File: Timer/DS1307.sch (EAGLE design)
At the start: 6 parts, among them IC10 DS1307, Q4 32.768

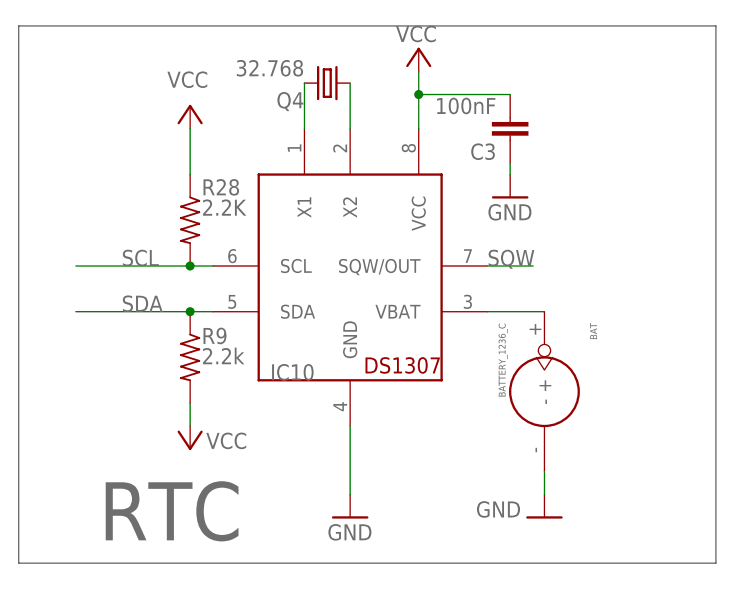
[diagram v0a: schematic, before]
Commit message: vcc updated in the circuit
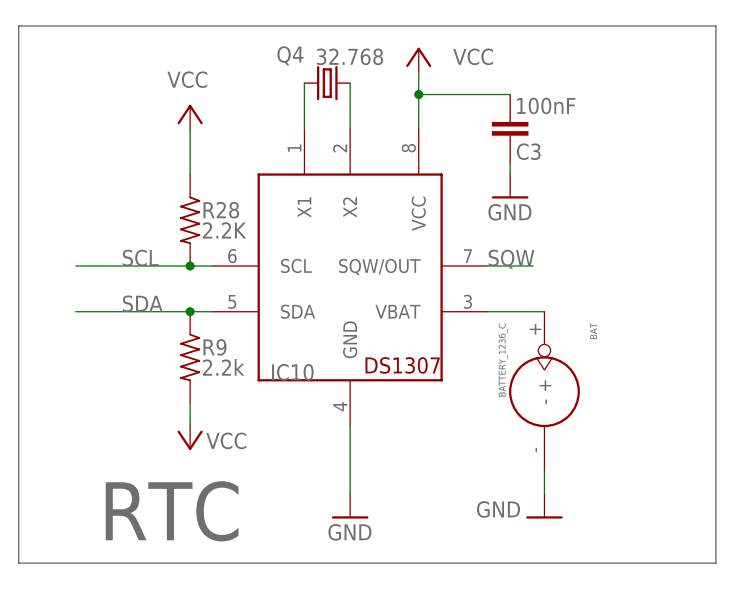
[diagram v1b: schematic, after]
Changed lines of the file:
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@@
 <layer number="94" name="Symbols" color="4" fill="1" visible="yes" active="yes"/>
 <layer number="95" name="Names" color="7" fill="1" visible="yes" active="yes"/>
-<layer number="96" name="Values" color="7" fill="1" visible="no" active="yes"/>
+<layer number="96" name="Values" color="7" fill="1" visible="yes" active="yes"/>
 <layer number="97" name="Info" color="7" fill="1" visible="yes" active="yes"/>
 <layer number="98" name="Guide" color="6" fill="1" visible="yes" active="yes"/>
@@
 <instances>
 <instance part="Q4" gate="G$1" x="-2.54" y="21.59" smashed="yes" rot="R180">
-<attribute name="NAME" x="-5.08" y="20.574" size="1.778" layer="95" rot="R180"/>
-<attribute name="VALUE" x="-5.08" y="24.13" size="1.778" layer="96" rot="R180"/>
+<attribute name="NAME" x="-5.08" y="25.654" size="1.778" layer="95" rot="R180"/>
+<attribute name="VALUE" x="3.81" y="25.4" size="1.778" layer="96" rot="R180"/>
 </instance>
 <instance part="IC10" gate="G$1" x="0" y="-1.27" smashed="yes">
@@
 </instance>
 <instance part="P+42" gate="VCC" x="7.62" y="25.4" smashed="yes" rot="MR0">
-<attribute name="VALUE" x="5.08" y="27.94" size="1.778" layer="96" rot="MR180"/>
+<attribute name="VALUE" x="11.43" y="25.4" size="1.778" layer="96" rot="MR180"/>
 </instance>
 <instance part="GND41" gate="1" x="0" y="-26.67" smashed="yes">
@@
 </instance>
 <instance part="R28" gate="G$1" x="-17.78" y="6.35" smashed="yes" rot="R270">
-<attribute name="NAME" x="-16.51" y="9.1186" size="1.778" layer="95"/>
-<attribute name="VALUE" x="-16.51" y="6.858" size="1.778" layer="96"/>
+<attribute name="NAME" x="-16.51" y="6.5786" size="1.778" layer="95"/>
+<attribute name="VALUE" x="-16.51" y="4.318" size="1.778" layer="96"/>
 </instance>
 <instance part="R9" gate="G$1" x="-17.78" y="-8.89" smashed="yes" rot="R270">
-<attribute name="NAME" x="-16.51" y="-7.3914" size="1.778" layer="95"/>
-<attribute name="VALUE" x="-16.51" y="-9.652" size="1.778" layer="96"/>
+<attribute name="NAME" x="-16.51" y="-8.6614" size="1.778" layer="95"/>
+<attribute name="VALUE" x="-16.51" y="-10.922" size="1.778" layer="96"/>
 </instance>
 <instance part="P+43" gate="VCC" x="-17.78" y="19.05" smashed="yes" rot="MR0">
@@
 </instance>
 <instance part="C3" gate="G$1" x="17.78" y="15.24" smashed="yes" rot="R180">
-<attribute name="NAME" x="16.256" y="14.859" size="1.778" layer="95" rot="R180"/>
-<attribute name="VALUE" x="16.256" y="19.939" size="1.778" layer="96" rot="R180"/>
+<attribute name="NAME" x="21.336" y="14.859" size="1.778" layer="95" rot="R180"/>
+<attribute name="VALUE" x="25.146" y="19.939" size="1.778" layer="96" rot="R180"/>
 </instance>
 <instance part="GND8" gate="1" x="17.78" y="8.89" smashed="yes">
